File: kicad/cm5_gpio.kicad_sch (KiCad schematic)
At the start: 14 parts, among them IC4 MAX98357AETE+T, J6 Conn_01x03, J7 SM04B-SRSS-TBLFSN, J8 SM04B-SRSS-TBLFSN, SW1 218-2LPSTRF

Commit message: finish first pcb revision
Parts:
- added C46: 0.1uF, Capacitor_SMD:C_0201_0603Metric, symbol Device:C
- added D15, D16, D21, D22, D9: TPD1E05U06DPYR, TPD1E05U06DPYR:SON65P60X100X45-2N, symbol TPD1E05U06DPYR:TPD1E05U06DPYR
- C35: footprint (none) -> Capacitor_SMD:C_0603_1608Metric
- C36: footprint (none) -> Capacitor_SMD:C_0201_0603Metric
- IC4: footprint (none) -> MAX98357AETE+T:QFN50P300X300X80-17N
- J6: footprint (none) -> Connector_PinHeader_2.54mm:PinHeader_1x03_P2.54mm_Vertical
- J7, J8: footprint (none) -> SM04B-SRSS-TB:CONN_SM04B_JST
- Module1: footprint CM5IO:Raspberry-Pi-5-Compute-Module -> CM5:Raspberry-Pi-5-Compute-Module
- R15: footprint (none) -> Resistor_SMD:R_0201_0603Metric
- R21, R25, R28: footprint Resistor_SMD:R_0402_1005Metric -> Resistor_SMD:R_0201_0603Metric
- SW1: footprint (none) -> 218_2LPSTRF:218-2-GULLWING_CTS
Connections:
- net 3.3V: now also C46.1
- net 5V: now also D9.1
- net GND: now also J7.5, J7.6, J8.5, J8.6, C46.2, D15.2, D16.2, D21.2, D22.2, D9.2
- net PWM: now also D16.1
- net TACHO: now also D15.1
- net UART0_RX: now also D21.1
- net UART0_TX: now also D22.1
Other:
- note added: "QUESTION: Need ESD protection on speaker amplifier outputs?"
- moved on the sheet: C35, C36, IC4, J6, R15, R25

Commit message: add docs and cleanup
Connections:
- net GND: now also Module1.91 (BT_nDisable)
- no-connect marks 41 -> 40
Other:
- note added: "TODO: Consider adding rtc battery"
- moved on the sheet: C35, C36
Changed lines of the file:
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@@
 	(generator_version "9.0")
 	(paper "A4")
+	(text "TODO: Consider adding\nrtc battery"
+		(exclude_from_sim no)
+		(at 41.402 118.364 0)
+		(effects
+			(font
+				(size 1.27 1.27)
+			)
+		)
+	)
 	(text "Pullup added for\nFans that don't have a\nstrong internal pullup "
 		(exclude_from_sim no)
@@
 	(text "QUESTION: Need ESD protection\non speaker amplifier outputs?"
 		(exclude_from_sim no)
-		(at 265.938 116.332 0)
+		(at 265.938 122.174 0)
 		(effects
 			(font
@@
 	(text "Left word\noutput only"
 		(exclude_from_sim no)
-		(at 212.09 120.904 0)
+		(at 211.836 122.428 0)
 		(effects
 			(font
@@
 	(text_box "Speaker"
 		(exclude_from_sim no)
-		(at 231.14 92.71 0)
+		(at 231.14 85.09 0)
 		(size 10.16 3.81)
 		(margins 0.9525 0.9525 0.9525 0.9525)
@@
 	)
 	(junction
-		(at 236.22 105.41)
+		(at 236.22 97.79)
 		(diameter 0)
 		(color 0 0 0 0)
@@
 	)
 	(junction
-		(at 224.79 97.79)
-		(diameter 0)
-		(color 0 0 0 0)
-	)
-	(junction
 		(at 55.88 80.01)
 		(diameter 1.016)
@@
 	)
 	(junction
-		(at 229.87 97.79)
+		(at 119.38 143.51)
+		(diameter 0)
+		(color 0 0 0 0)
+	)
+	(junction
+		(at 229.87 90.17)
 		(diameter 0)
 		(color 0 0 0 0)
@@
 	)
 	(junction
+		(at 224.79 90.17)
+		(diameter 0)
+		(color 0 0 0 0)
+	)
+	(junction
 		(at 224.79 109.22)
 		(diameter 0)
@@
 	)
 	(no_connect
-		(at 118.11 143.51)
-	)
-	(no_connect
 		(at 57.15 87.63)
 	)
@@
 	(wire
 		(pts
-			(xy 236.22 105.41) (xy 242.57 105.41)
+			(xy 236.22 97.79) (xy 242.57 97.79)
 		)
 		(stroke
@@
 	(wire
 		(pts
+			(xy 118.11 143.51) (xy 119.38 143.51)
+		)
+		(stroke
+			(width 0)
+			(type default)
+		)
+	)
+	(wire
+		(pts
 			(xy 55.88 151.13) (xy 55.88 158.75)
 		)
@@
 	(wire
 		(pts
-			(xy 119.38 118.11) (xy 119.38 158.75)
+			(xy 119.38 118.11) (xy 119.38 143.51)
 		)
 		(stroke
@@
 	(wire
 		(pts
+			(xy 119.38 143.51) (xy 119.38 158.75)
+		)
+		(stroke
+			(width 0)
+			(type solid)
+		)
+	)
+	(wire
+		(pts
 			(xy 55.88 80.01) (xy 57.15 80.01)
 		)
@@
 	(wire
 		(pts
-			(xy 229.87 105.41) (xy 236.22 105.41)
+			(xy 229.87 97.79) (xy 236.22 97.79)
 		)
 		(stroke
@@
 	(wire
 		(pts
-			(xy 224.79 97.79) (xy 224.79 109.22)
+			(xy 224.79 90.17) (xy 224.79 109.22)
 		)
 		(stroke
@@
 	(wire
 		(pts
-			(xy 236.22 105.41) (xy 236.22 106.68)
+			(xy 236.22 97.79) (xy 236.22 99.06)
 		)
 		(stroke
@@
 	(wire
 		(pts
-			(xy 224.79 95.25) (xy 224.79 97.79)
+			(xy 224.79 87.63) (xy 224.79 90.17)
 		)
 		(stroke
@@
 	(wire
 		(pts
-			(xy 224.79 97.79) (xy 229.87 97.79)
+			(xy 224.79 90.17) (xy 229.87 90.17)
 		)
 		(stroke
@@
 	(wire
 		(pts
-			(xy 229.87 97.79) (xy 242.57 97.79)
+			(xy 229.87 90.17) (xy 242.57 90.17)
 		)
 		(stroke
@@
 	(hierarchical_label "5V"
 		(shape input)
-		(at 224.79 95.25 90)
+		(at 224.79 87.63 90)
 		(effects
 			(font
@@
 	(hierarchical_label "GND"
 		(shape passive)
-		(at 236.22 106.68 270)
+		(at 236.22 99.06 270)
 		(effects
 			(font
@@
 	(symbol
 		(lib_id "Device:C")
-		(at 229.87 101.6 0)
+		(at 229.87 93.98 0)
 		(unit 1)
 		(exclude_from_sim no)
@@
 		(on_board yes)
 		(dnp no)
-		(fields_autoplaced yes)
 		(property "Reference" "C35"
-			(at 233.68 100.3299 0)
+			(at 233.68 92.7099 0)
 			(effects
 				(font
@@
 		)
 		(property "Value" "10uF"
-			(at 233.68 102.8699 0)
+			(at 233.68 95.2499 0)
 			(effects
 				(font
@@
 		)
 		(property "Footprint" "Capacitor_SMD:C_0603_1608Metric"
-			(at 230.8352 105.41 0)
+			(at 230.8352 97.79 0)
 			(effects
 				(font
@@
 		)
 		(property "Datasheet" "~"
-			(at 229.87 101.6 0)
+			(at 229.87 93.98 0)
 			(effects
 				(font
@@
 		)
 		(property "Description" "Unpolarized capacitor"
-			(at 229.87 101.6 0)
+			(at 229.87 93.98 0)
 			(effects
 				(font
@@
 	(symbol
 		(lib_id "Device:C")
-		(at 242.57 101.6 0)
+		(at 242.57 93.98 0)
 		(unit 1)
 		(exclude_from_sim no)
@@
 		(fields_autoplaced yes)
 		(property "Reference" "C36"
-			(at 246.38 100.3299 0)
+			(at 246.38 92.7099 0)
 			(effects
 				(font
@@
 		)
 		(property "Value" "0.1uF"
-			(at 246.38 102.8699 0)
+			(at 246.38 95.2499 0)
 			(effects
 				(font
@@
 		)
 		(property "Footprint" "Capacitor_SMD:C_0201_0603Metric"
-			(at 243.5352 105.41 0)
+			(at 243.5352 97.79 0)
 			(effects
 				(font
@@
 		)
 		(property "Datasheet" "~"
-			(at 242.57 101.6 0)
+			(at 242.57 93.98 0)
 			(effects
 				(font
@@
 		)
 		(property "Description" "Unpolarized capacitor"
-			(at 242.57 101.6 0)
+			(at 242.57 93.98 0)
 			(effects
 				(font
@@
 		(on_board yes)
 		(dnp no)
-		(fields_autoplaced yes)
 		(property "Reference" "IC4"
-			(at 257.81 121.8498 0)
+			(at 240.03 109.728 0)
 			(effects
 				(font
@@
 		)
 		(property "Value" "MAX98357AETE+T"
-			(at 257.81 124.3898 0)
+			(at 240.03 112.268 0)
 			(effects
 				(font

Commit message: add power testpoints, add debug gpio testpoints, add comms testpoints, add logo, add component orientation silkscreen, add board name and revision silkscreen
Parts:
- added TP1, TP17, TP18, TP2, TP3, TP4: TestPoint, TestPoint:TestPoint_Pad_1.0x1.0mm, symbol Connector:TestPoint
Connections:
- net PCM_CLK: now also TP2.1
- net PCM_DOUT: now also TP4.1
- net PCM_FS: now also TP3.1
- net SD_MODE: now also TP1.1
- net TEST_GPIO_1: now reaches Module1.45 (GPIO24)
- net TEST_GPIO_1: now also TP17.1
- net TEST_GPIO_2: now reaches Module1.47 (GPIO23)
- net TEST_GPIO_2: now also TP18.1
- no-connect marks 40 -> 38

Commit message: generate manufacturing files, final checks, cleanup
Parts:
- removed Module1: ComputeModule5-CM5, CM5:Raspberry-Pi-5-Compute-Module, symbol CM5IO:ComputeModule5-CM5
- added J11: 10164227-1001A1RLF, 10164227-1001A1RLF:101642271001A1RLF, symbol 10164227-1001A1RLF:10164227-1001A1RLF
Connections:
- net 1.8V: now also J11.88 (+1.8v_(Output)_600mA_Max), J11.90 (+1.8v_(Output)_600mA_Max)
- net 3.3V: now also J11.78 (GPIO_VREF(1.8v/3.3v_Input))
- net 5V: now also J11.77 (+5v_(Input)), J11.79 (+5v_(Input)), J11.81 (+5v_(Input)), J11.83 (+5v_(Input)), J11.85 (+5v_(Input)), J11.87 (+5v_(Input))
- net CAM_GPIO0: now also J11.97 (CAM_GPIO0)
- net CAM_GPIO1: now also J11.100 (CAM_GPIO1)
- net CC1: now also J11.94 (CC1)
- net CC2: now also J11.96 (CC2)
- net EEPROM_nWP: now also J11.20 (EEPROM_nWP)
- net GND: now also J11.1 (GND), J11.13 (GND), J11.14 (GND), J11.2 (GND), J11.22 (GND), J11.23 (GND), J11.32 (GND), J11.33 (GND), J11.42 (GND), J11.43 (GND), J11.52 (GND), J11.53 (GND), J11.59 (GND), J11.60 (GND), J11.65 (GND), J11.66 (GND), J11.7 (GND), J11.71 (GND), J11.74 (GND), J11.8 (GND), J11.91 (BT_nDisable), J11.92 (PWR_BUT), J11.98 (GND)
- net ID_SC: now also J11.35 (ID_SC)
- net ID_SD: now also J11.36 (ID_SD)
- net IR_LED_DIM: now also J11.28 (GPIO13)
- net LASER1: now also J11.44 (GPIO10)
- net LASER2: now also J11.46 (GPIO22)
- net PCM_CLK: now also J11.49 (GPIO18)
- net PCM_DOUT: now also J11.25 (GPIO21)
- net PCM_FS: now also J11.26 (GPIO19)
- net PLATFORM_I2C_SCL: now also J11.56 (GPIO3)
- net PLATFORM_I2C_SDA: now also J11.58 (GPIO2)
- net PWM: now also J11.19 (FAN_PWM)
- net SCL0: now also J11.80 (SCL0)
- net SDA0: now also J11.82 (SDA0)
- net SIM_I2C_SCL: now also J11.40 (GPIO9)
- net SIM_I2C_SDA: now also J11.39 (GPIO8)
- net SIM_PWR_OFF: now also J11.29 (GPIO16)
- net SIM_RESET_IN: now also J11.50 (GPIO17)
- net SIM_UART_DTR: now also J11.38 (GPIO11)
- net TACHO: now also J11.16 (FAN_TACHO)
- net TEST_GPIO_1: now also J11.45 (GPIO24)
- net TEST_GPIO_2: now also J11.47 (GPIO23)
- net UART0_RX: now also J11.51 (GPIO15)
- net UART0_TX: now also J11.55 (GPIO14)
- net UART2_CTS: now also J11.30 (GPIO6)
- net UART2_RTS: now also J11.37 (GPIO7)
- net UART2_RX: now also J11.34 (GPIO5)
- net UART2_TX: now also J11.54 (GPIO4)
- net W_LED_DIM: now also J11.31 (GPIO12)
- net nPWR_LED: now also J11.95 (LED_nPWR)
- net nRPIBOOT: now also J11.93 (nRPIBOOT)
- net at R21.2: now also J11.21 (LED_nACT)

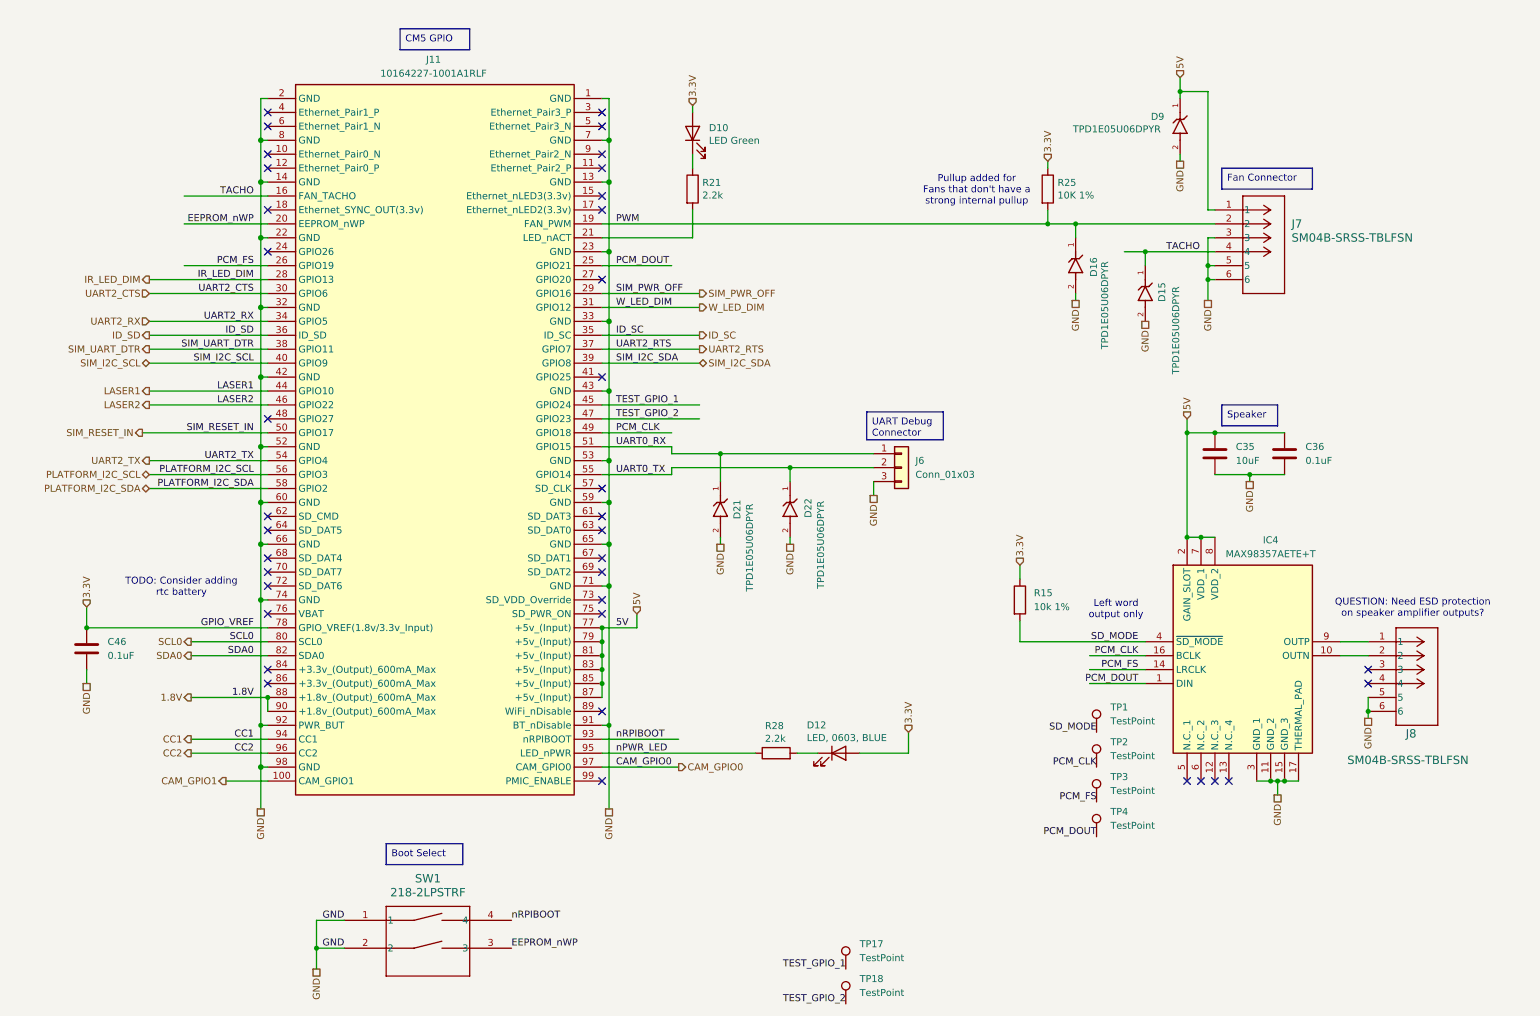
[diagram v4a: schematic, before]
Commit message: add can controller and transceiver, replace jst connectors with molex micro fit connectors
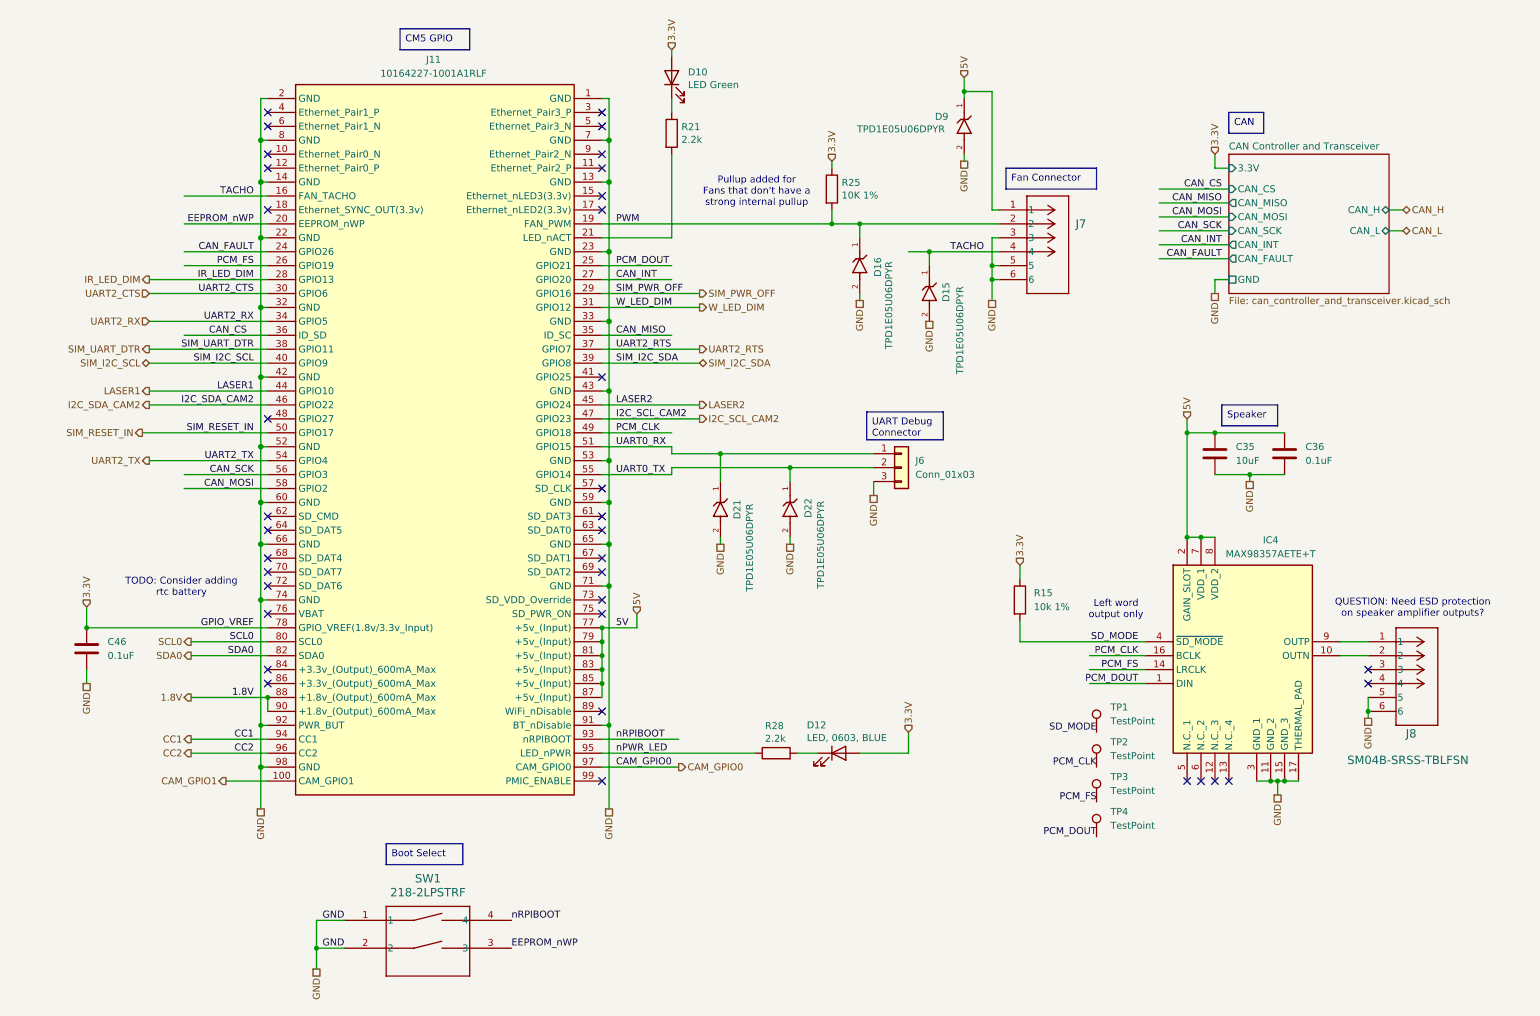
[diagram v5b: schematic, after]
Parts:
- removed TP17, TP18: TestPoint, TestPoint:TestPoint_Pad_1.0x1.0mm, symbol Connector:TestPoint
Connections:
- net TEST_GPIO_1 is gone; now on net LASER2: J11.45 (GPIO24)
- net LASER2: no longer J11.46 (GPIO22)
- net CAN_FAULT: now reaches J11.24 (GPIO26)
- net CAN_INT: now reaches J11.27 (GPIO20)
- net ID_SC renamed CAN_MISO
- net ID_SD renamed CAN_CS
- net PLATFORM_I2C_SCL renamed CAN_SCK
- net PLATFORM_I2C_SDA renamed CAN_MOSI
- net TEST_GPIO_2 renamed I2C_SCL_CAM2
- new net I2C_SDA_CAM2: J11.46 (GPIO22)
- no-connect marks 38 -> 36
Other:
- added sheet CAN Controller and Transceiver (can_controller_and_transceiver.kicad_sch)
- moved on the sheet: D10, D15, D16, D9, J7, R21, R25

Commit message: add can controller and transceiver, replace platform power connector with one with more appropriate current rating, add return vias
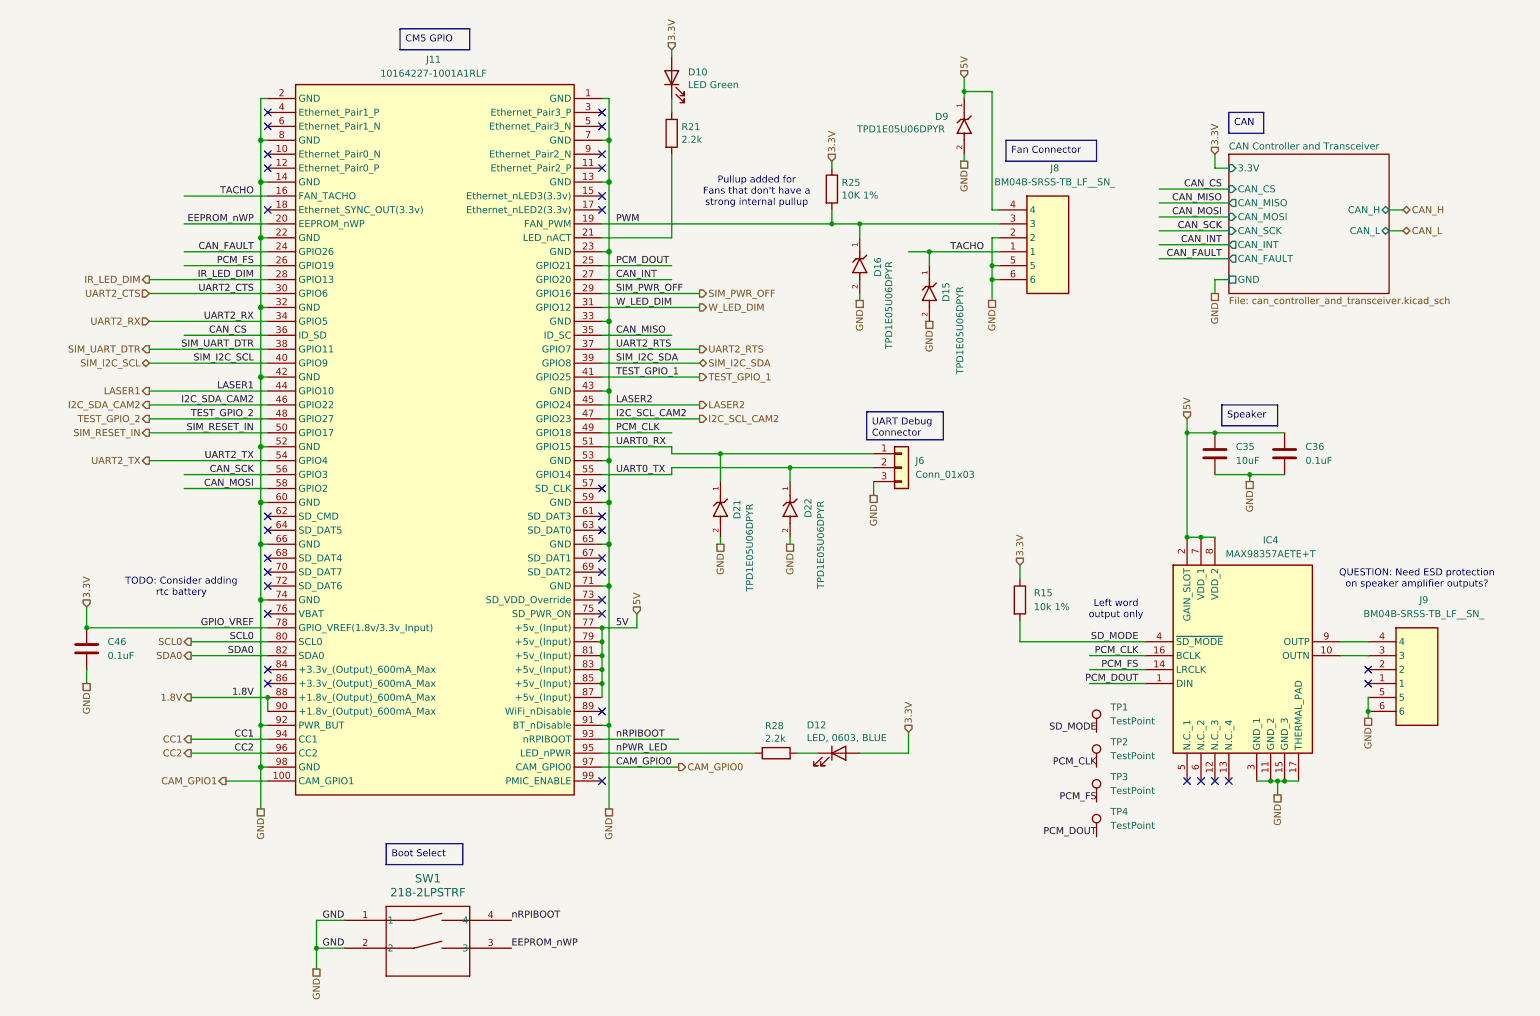
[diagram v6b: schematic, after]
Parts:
- removed J7, J8: SM04B-SRSS-TBLFSN, SM04B-SRSS-TB:CONN_SM04B_JST, symbol SM04B-SRSS-TB:SM04B-SRSS-TBLFSN
- added J8, J9: BM04B-SRSS-TB_LF__SN_, BM04B-SRSS-TB_LF__SN_:BM04B-SRSS-TB_LFSN_, symbol BM04B-SRSS-TB_LF__SN_:BM04B-SRSS-TB_LF__SN_
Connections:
- net 5V: now also J8.4
- net GND: now also J8.2, J8.5, J8.6, J9.5, J9.6
- net PWM: now also J8.3
- net TACHO: now also J8.1
- net TEST_GPIO_1: now reaches J11.41 (GPIO25)
- net TEST_GPIO_2: now reaches J11.48 (GPIO27)
- net at IC4.10 (OUTN): now also J9.3
- net at IC4.9 (OUTP): now also J9.4
- no-connect marks 36 -> 34
